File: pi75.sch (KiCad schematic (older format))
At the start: 173 parts, among them J1 Conn_2Rows-05Pins, K1 KEYSW-keyboard_parts, K10 KEYSW-keyboard_parts, K11 KEYSW-keyboard_parts, K12 KEYSW-keyboard_parts, K13 KEYSW-keyboard_parts, K14 KEYSW-keyboard_parts, K15 KEYSW-keyboard_parts, K16 KEYSW-keyboard_parts, K17 KEYSW-keyboard_parts, K18 KEYSW-keyboard_parts, K19 KEYSW-keyboard_parts, K2 KEYSW-keyboard_parts, K20 KEYSW-keyboard_parts, K21 KEYSW-keyboard_parts, K22 KEYSW-keyboard_parts, K23 KEYSW-keyboard_parts, K24 KEYSW-keyboard_parts, K25 KEYSW-keyboard_parts, K26 KEYSW-keyboard_parts, K27 KEYSW-keyboard_parts, K28 KEYSW-keyboard_parts, K29 KEYSW-keyboard_parts, K3 KEYSW-keyboard_parts, K30 KEYSW-keyboard_parts, K31 KEYSW-keyboard_parts, K32 KEYSW-keyboard_parts, K33 KEYSW-keyboard_parts, K34 KEYSW-keyboard_parts, K35 KEYSW-keyboard_parts, K36 KEYSW-keyboard_parts, K37 KEYSW-keyboard_parts, K38 KEYSW-keyboard_parts, K39 KEYSW-keyboard_parts, K4 KEYSW-keyboard_parts, K40 KEYSW-keyboard_parts, K41 KEYSW-keyboard_parts, K42 KEYSW-keyboard_parts, K43 KEYSW-keyboard_parts, K44 KEYSW-keyboard_parts, K45 KEYSW-keyboard_parts, K46 KEYSW-keyboard_parts, K47 KEYSW-keyboard_parts, K48 KEYSW-keyboard_parts, K49 KEYSW-keyboard_parts, K5 KEYSW-keyboard_parts, K50 KEYSW-keyboard_parts, K51 KEYSW-keyboard_parts, K52 KEYSW-keyboard_parts, K53 KEYSW-keyboard_parts, K54 KEYSW-keyboard_parts, K55 KEYSW-keyboard_parts, K56 KEYSW-keyboard_parts, K57 KEYSW-keyboard_parts, K58 KEYSW-keyboard_parts, K59 KEYSW-keyboard_parts, K6 KEYSW-keyboard_parts, K60 KEYSW-keyboard_parts, K61 KEYSW-keyboard_parts, K62 KEYSW-keyboard_parts, K63 KEYSW-keyboard_parts, K64 KEYSW-keyboard_parts, K65 KEYSW-keyboard_parts, K66 KEYSW-keyboard_parts, K67 KEYSW-keyboard_parts, K68 KEYSW-keyboard_parts, K69 KEYSW-keyboard_parts, K7 KEYSW-keyboard_parts, K70 KEYSW-keyboard_parts, K71 KEYSW-keyboard_parts, K72 KEYSW-keyboard_parts, K73 KEYSW-keyboard_parts, K74 KEYSW-keyboard_parts, K75 KEYSW-keyboard_parts, K76 KEYSW-keyboard_parts, K77 KEYSW-keyboard_parts, K78 KEYSW-keyboard_parts, K79 KEYSW-keyboard_parts, K8 KEYSW-keyboard_parts, K80 KEYSW-keyboard_parts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

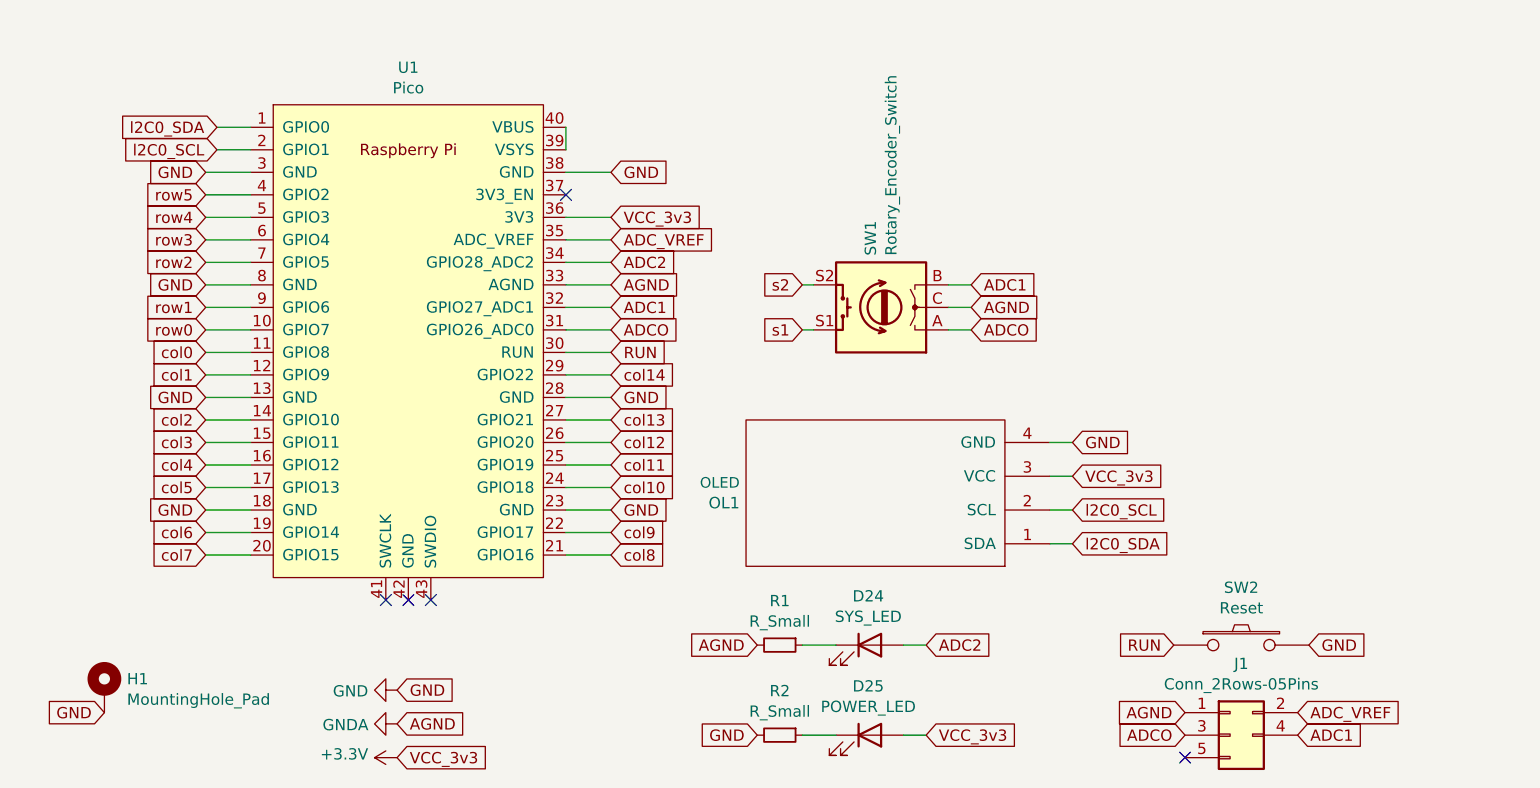
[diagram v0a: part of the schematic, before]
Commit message: Cleaned up schematic
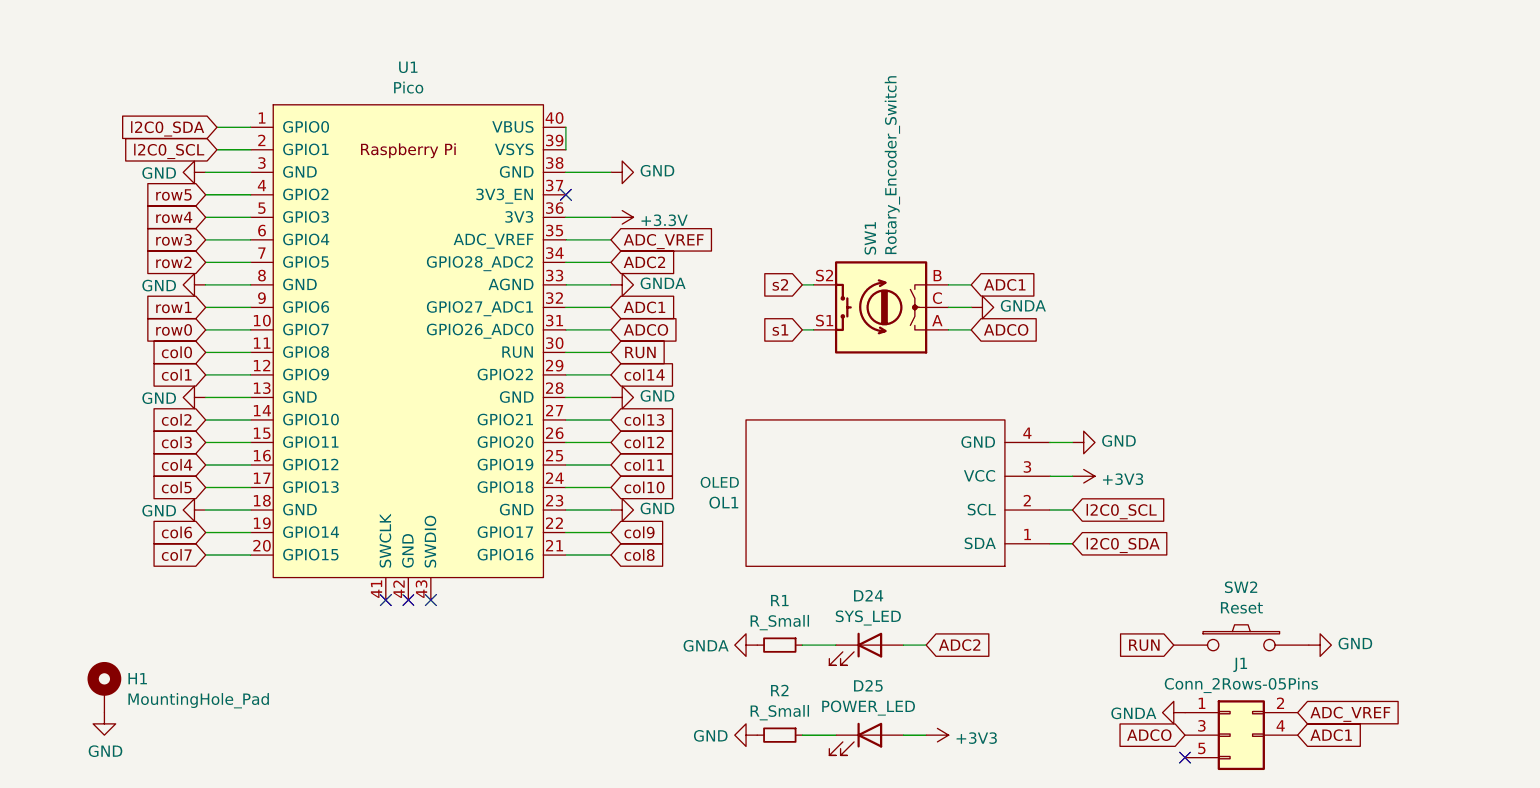
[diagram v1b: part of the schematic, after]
